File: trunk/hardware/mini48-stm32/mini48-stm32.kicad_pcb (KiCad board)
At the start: 2 copper layers, 78.9 x 19.8 mm, 34 parts, among them J1 MINI-USB, P1 CONN_20, P2 CONN_20, Q1 DTA114E, SW1 Reset, SW2 But, U1 STM32F103C8, U2 STF202, U3 LM2937, X1 8MHz, X2 32768KHz

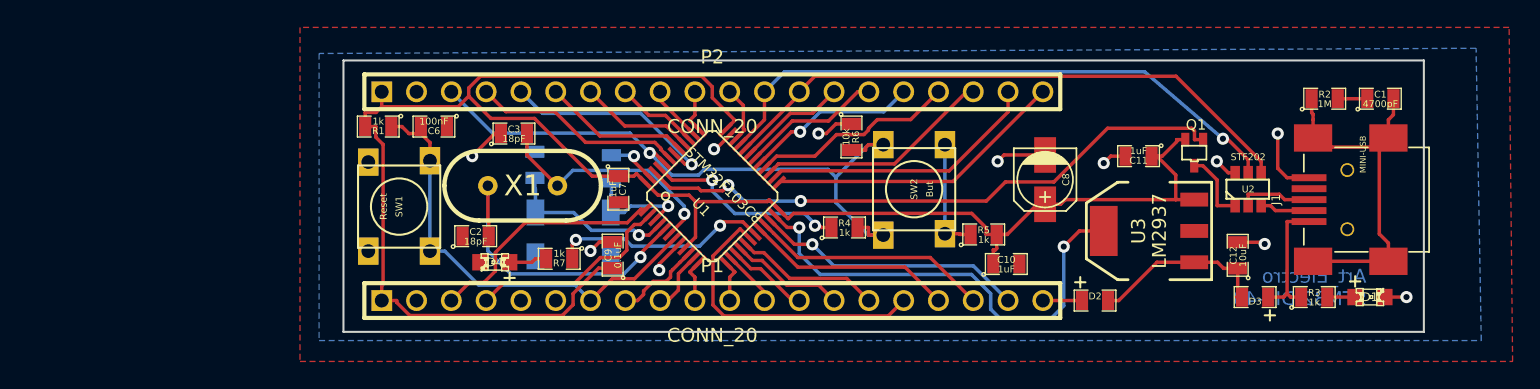
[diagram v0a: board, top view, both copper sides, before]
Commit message: unified USB filter
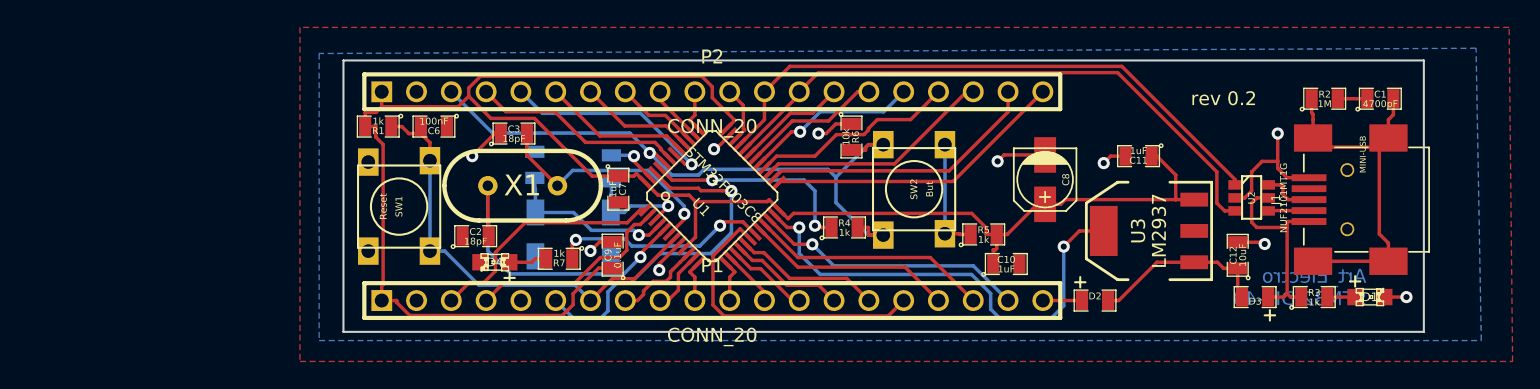
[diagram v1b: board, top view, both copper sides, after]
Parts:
- removed Q1: DTA114E, SOT323
- U2: value STF202 -> NUF2101MT1G
- moved U2 0.68 mm to (175.8, 89.0), turned to 270 degrees
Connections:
- P1 pad 6: (no net) -> /35
- U1 pad 46: /DISK -> /35
- U2 pad 1: N-0000015 (its old number) -> /23_USBDP
- U2 pad 2: /D+ -> GND
- U2 pad 3: /D- -> /24_USBDM
- U2 pad 4: /24_USBDM -> /D-
- U2 pad 5: /23_USBDP -> /+5v
- U2 pad 6: GND -> /D+
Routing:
- net /DISK: track 44.0 -> 0.00 mm, vias 2 -> 0
- net /35: track 0.00 -> 25.9 mm, vias 0 -> 1
- net /+5v: track 9.48 -> 15.0 mm
- net N-0000015 (its old number): track 5.29 -> 0.00 mm
- net GND: track 67.6 -> 71.0 mm, vias 14 -> 13
- net /VCC: track 138.3 -> 135.6 mm
- net /D+: track 5.44 -> 3.73 mm
- net N-0000053: track 15.1 -> 16.2 mm
- net /D-: track 3.64 -> 3.00 mm
- net /23_USBDP: track 43.9 -> 43.5 mm, vias 1 -> 0
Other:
- board text added: "rev 0.2"

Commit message: 
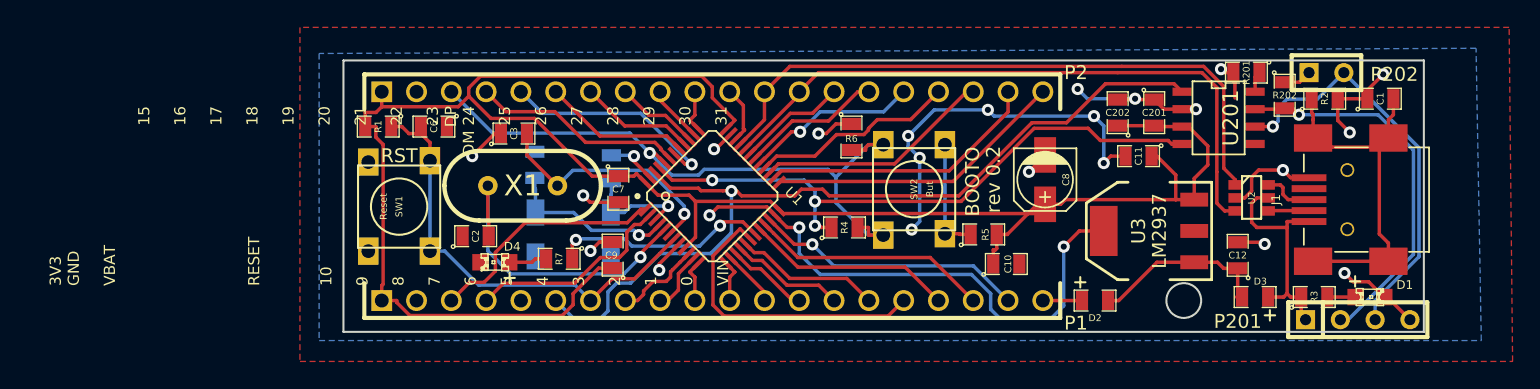
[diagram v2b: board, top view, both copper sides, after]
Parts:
- added C201: 0.1uF, SM0805, F.Cu at (168.7, 82.8)
- added C202: 4.7uF, SM0805, F.Cu at (166.0, 82.8)
- added P201: CONN_4, SIL-4, F.Cu at (183.5, 97.9)
- added P202: JUMPER, JUMPER-2, F.Cu at (181.2, 79.9)
- added R201: 10k, SM0805, F.Cu at (175.4, 79.9)
- added R202: 120, SM0805, F.Cu at (178.2, 81.5)
- added U201: SN65HVD230, SO8E, F.Cu at (173.4, 83.2)
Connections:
- net /+5v renamed /CAN BUS/5V
- net /35 renamed /CAN BUS/CAN_TX
- net /VCC renamed /CAN BUS/3.3V
- R4 pad 1: N-0000053 (its old number) -> /CAN BUS/CAN_RX
- U1 pad 45: N-0000053 (its old number) -> /CAN BUS/CAN_RX
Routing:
- net GND: track 71.0 -> 122.7 mm, vias 13 -> 26
- net /CAN BUS/CAN_RX: track 0.00 -> 45.7 mm, vias 0 -> 3
- net /CAN BUS/CAN_TX: track 25.9 -> 62.9 mm
- net /CAN BUS/CANL: track 0.00 -> 30.3 mm, vias 0 -> 1
- net /CAN BUS/CANH: track 0.00 -> 27.8 mm, vias 0 -> 1
- net N-0000053 (its old number): track 16.2 -> 0.00 mm, vias 2 -> 0
- net /CAN BUS/3.3V: track 135.6 -> 149.7 mm
- net /24_USBDM: track 43.8 -> 47.4 mm
- net /23_USBDP: track 43.5 -> 47.0 mm
- net N-0000056: track 0.00 -> 2.07 mm
- net /CAN BUS/5V: track 15.0 -> 16.8 mm
- net N-0000057: track 0.00 -> 1.53 mm
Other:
- outline, holes or cut-outs redrawn
- board text added: "15 16 17 18 19 20 21 22 23 DP DM 24 25 26 27 28 29 30 31"
- board text added: "3V3 GND BOOTO 15 16 17 18 19 20 21 22 23 USBDP 24 USBDM 25 26 27 28 29 30 31"
- board text added: "3V3 GND VBAT 14 NC CANTX 35 RESET 11 10 9 8 7 6 5 4 3 2 1 0 VIN"
- board text added: "3V3 GND VBAT RESET 10 9 8 7 6 5 4 3 2 1 0 VIN"
- board text added: "5V CANH CANL GND"
- board text added: "BOOTO"
- board text added: "CAN 120"
- board text added: "RST"

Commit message: 
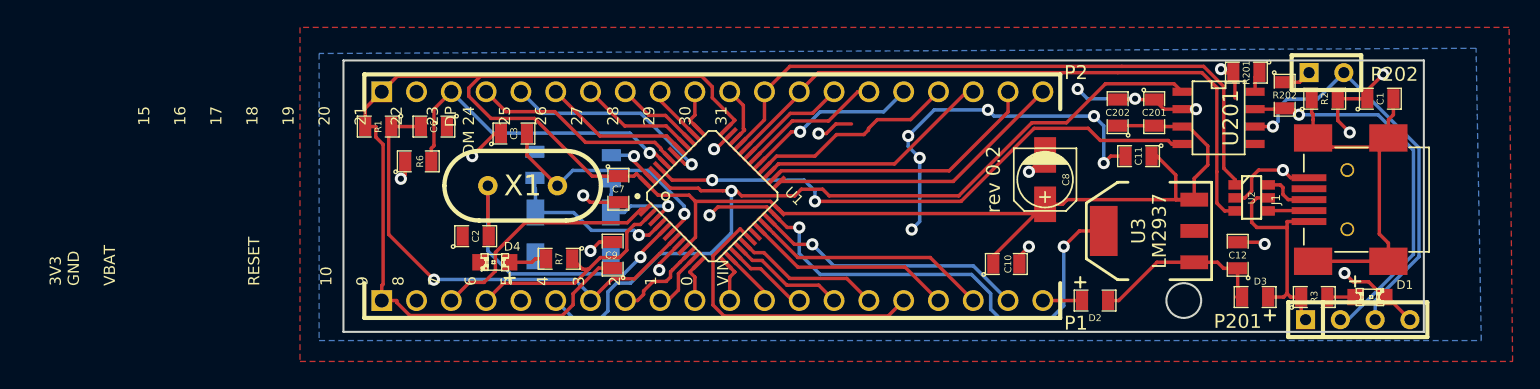
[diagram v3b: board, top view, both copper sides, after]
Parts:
- removed R4, R5: 1k, SM0805
- removed SW1: Reset, TL-1105
- removed SW2: But, TL-1105
- moved R6 31.7 mm to (114.9, 86.4), turned to 0 degrees
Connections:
- R7 pad 1: /33 -> /14
- U1 pad 19: /33 -> (no net)
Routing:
- net /BOOT0: track 48.2 -> 23.5 mm
- net /33: track 15.9 -> 0.00 mm, vias 2 -> 0
- net N-0000055: track 8.42 -> 0.00 mm
- net /CAN BUS/CAN_RX: track 45.7 -> 42.5 mm, vias 3 -> 2
- net (no net): track 0.00 -> 2.70 mm, vias 0 -> 1
- net /Reset: track 33.0 -> 35.1 mm, vias 0 -> 1
- net /14: track 15.4 -> 16.9 mm
- net /CAN BUS/3.3V: track 149.7 -> 150.7 mm
- net GND: track 122.7 -> 122.9 mm, vias 26 -> 27
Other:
- board text removed: "BOOTO"
- board text removed: "RST"

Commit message: 
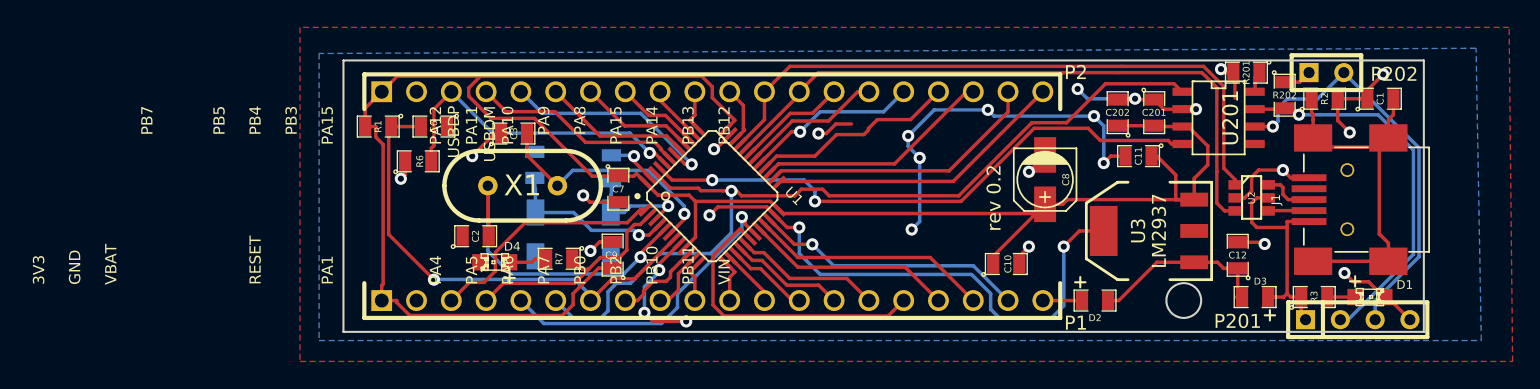
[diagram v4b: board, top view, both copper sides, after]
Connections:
- net /0 renamed /PB11
- net /1 renamed /PB10
- net /10 renamed /PA1
- net /11 renamed /PA0
- net /14 renamed /PC13
- net /15 renamed /PB7
- net /16 renamed /PB6
- net /17 renamed /PB5
- net /18 renamed /PB4
- net /19 renamed /PB3
- net /2 renamed /PB2
- net /20 renamed /PA15
- net /21 renamed /PA14
- net /22 renamed /PA13
- net /23_USBDP renamed /PA12_USBDP
- net /24_USBDM renamed /PA11_USBDM
- net /25 renamed /PA10
- net /26 renamed /PA9
- net /27 renamed /PA8
- net /28 renamed /PB15
- net /29 renamed /PB14
- net /3 renamed /PB0
- net /30 renamed /PB13
- net /31 renamed /PB12
- net /4 renamed /PA7
- net /5 renamed /PA6
- net /6 renamed /PA5
- net /7 renamed /PA4
- net /8 renamed /PA3
- net /9 renamed /PA2
- net /OSC32_IN renamed /PC14_OSC32_IN
- net /OSC32_OUT renamed /PC15_OSC32_OUT
- net N-0000052 renamed /PD1
- net N-0000053 renamed /PD0
- P1 pad 5: (no net) -> /PB1
- U1 pad 19: (no net) -> /PB1
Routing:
- net /PB1: track 0.00 -> 22.8 mm, vias 0 -> 1
- net GND: track 122.9 -> 129.8 mm, vias 27 -> 29
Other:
- board text added: "3V3 GND BOOTO PB7 PB6 PB5 PB4 PB3 PA15 PA14 PA13 PA12 USBDP PA11 USBDM PA10 PA9 PA8 PA15 PA14 PB13 PB12"
- board text added: "3V3 GND VBAT PC13 PB1 CANTX PB9 RESET PA0 PA1 PA2 PA3 PA4 PA5 PA6 PA7 PB0 PB2 PB10 PB11 VIN"
- board text added: "3V3 GND VBAT RESET PA1 PA4 PA5 PA6 PA7 PB0 PB2 PB10 PB11 VIN"
- board text added: "PB7 PB5 PB4 PB3 PA15 PA12 USBDP PA11 USBDM PA10 PA9 PA8 PA15 PA14 PB13 PB12"
- board text removed: "15 16 17 18 19 20 21 22 23 DP DM 24 25 26 27 28 29 30 31"
- board text removed: "3V3 GND BOOTO 15 16 17 18 19 20 21 22 23 USBDP 24 USBDM 25 26 27 28 29 30 31"
- board text removed: "3V3 GND VBAT 14 NC CANTX 35 RESET 11 10 9 8 7 6 5 4 3 2 1 0 VIN"
- board text removed: "3V3 GND VBAT RESET 10 9 8 7 6 5 4 3 2 1 0 VIN"
